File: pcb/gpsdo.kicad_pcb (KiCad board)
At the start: 4 copper layers, 140 x 100 mm, 161 parts, among them IC1 ICE40LP384-SG32, J1 JTAG, J10 CLK0, J11 CLK7, J12 USB_B_Micro, J13 CLK6, J14 CLK5, J15 CLK4, J16 RF_Shield_One_Piece, J2 SSD1306, J3 EXT_CLOCK, J5 USB_B_Micro, J6 CLK3, J7 Screw_Terminal_01x03, J8 CLK2, J9 CLK1, M1 E73-2G4M08S1C-52840, Q1 S9018, SW1 EC11, SW2 MCML4-112B, U1 MCP9808_MSOP, U2 MCP9808_MSOP, U3 TPS652510, U4 LT1763xS8, U5 74LVC1G17, U6 Si5351C-B-GM, U7 74LVC1G17, U8 uBlox NEO-7M, U9 AD5761R, Y1 32768, Y2 8663-XS

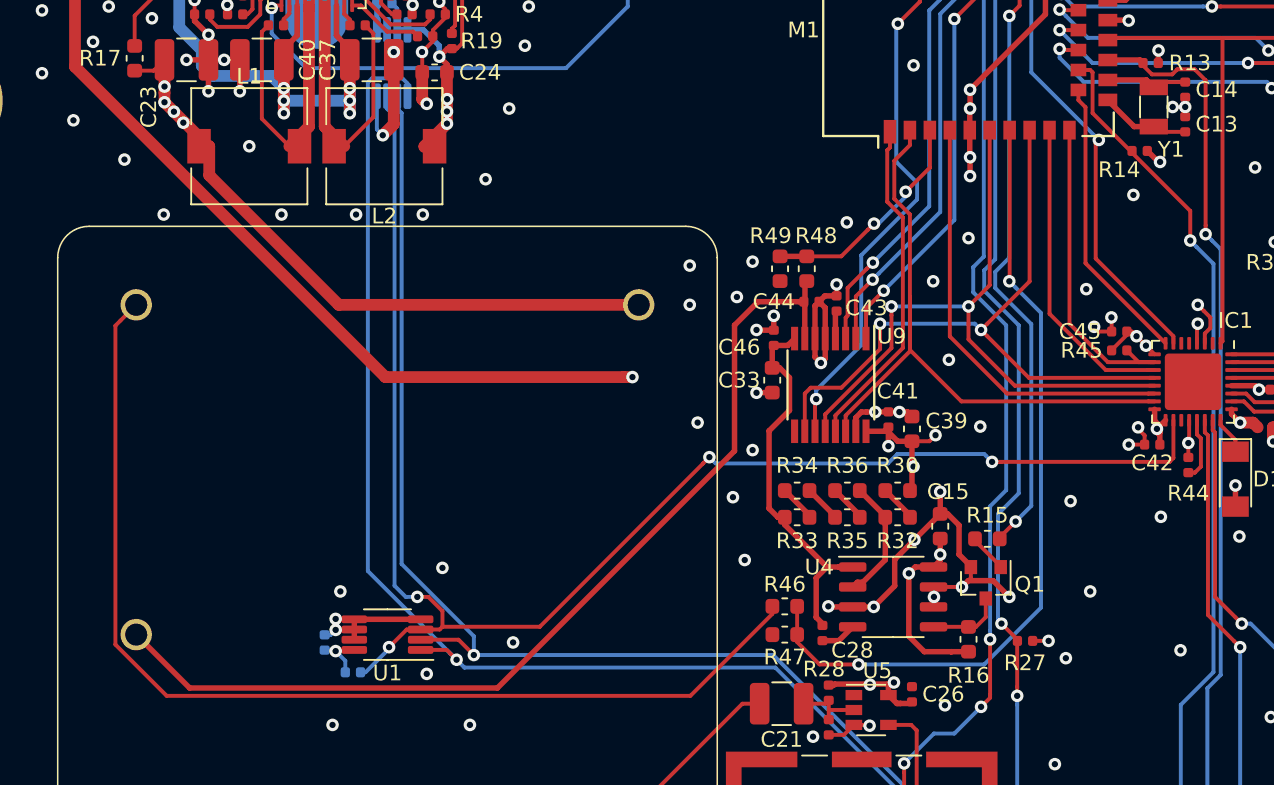
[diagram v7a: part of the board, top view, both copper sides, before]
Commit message: increase distance of DAC output rail to any noisy digital signal
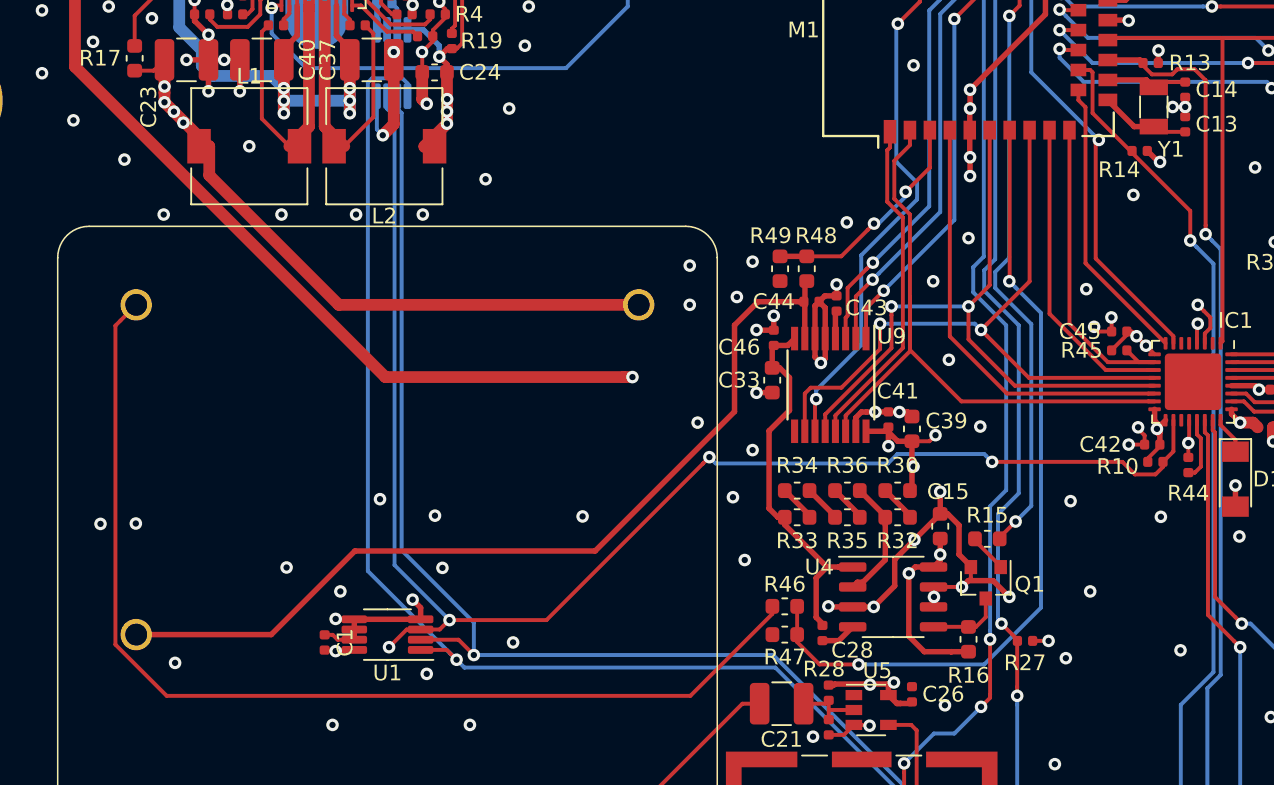
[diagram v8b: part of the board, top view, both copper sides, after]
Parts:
- C1, R10: moved to F.Cu
- moved R10 52.8 mm to (112.9, 89.0)
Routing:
- net Net-(C44-Pad1): track 62.5 -> 58.2 mm
- net /TEMP_ALERT: track 96.8 -> 93.9 mm
- net GND: track 431.5 -> 432.9 mm, vias 220 -> 227
- net +3V3: track 78.7 -> 79.7 mm
